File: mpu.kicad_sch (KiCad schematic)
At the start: 27 parts, among them J12 Conn_01x06, U2 STM32U585CIUxQ, Y1 ECS-160-8-36B2-CKM-TR, Y2 CM7V-T1A-32.768KHZ

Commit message: worked mainly on pcb
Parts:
- removed J12: Conn_01x06, Connector_PinHeader_2.54mm:PinHeader_1x06_P2.54mm_Vertical, symbol Connector_Generic:Conn_01x06
- added J13: Conn_01x04, Connector_PinHeader_2.54mm:PinHeader_1x04_P2.54mm_Vertical, symbol Connector_Generic:Conn_01x04
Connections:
- net servo1: now also J13.1 (Pin_1)
- net servo2: now also J13.2 (Pin_2)
- net servo3: now also J13.3 (Pin_3)
- net servo4: now also J13.4 (Pin_4)
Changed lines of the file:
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@@
 	(wire
 		(pts
-			(xy 163.83 76.2) (xy 163.83 77.47)
-		)
-		(stroke
-			(width 0)
-			(type default)
-		)
-	)
-	(wire
-		(pts
 			(xy 111.76 125.73) (xy 113.03 125.73)
 		)
@@
 	(wire
 		(pts
-			(xy 158.75 90.17) (xy 160.02 90.17)
-		)
-		(stroke
-			(width 0)
-			(type default)
-		)
-	)
-	(wire
-		(pts
 			(xy 109.22 80.01) (xy 113.03 80.01)
 		)
@@
 	(wire
 		(pts
-			(xy 163.83 93.98) (xy 163.83 90.17)
-		)
-		(stroke
-			(width 0)
-			(type default)
-		)
-	)
-	(wire
-		(pts
 			(xy 138.43 72.39) (xy 138.43 71.12)
 		)
@@
 	(wire
 		(pts
-			(xy 163.83 90.17) (xy 165.1 90.17)
-		)
-		(stroke
-			(width 0)
-			(type default)
-		)
-	)
-	(wire
-		(pts
 			(xy 58.42 87.63) (xy 58.42 92.71)
 		)
@@
 	(wire
 		(pts
-			(xy 140.97 49.53) (xy 140.97 50.8)
+			(xy 158.75 90.17) (xy 160.02 90.17)
 		)
 		(stroke
@@
 	(wire
 		(pts
-			(xy 138.43 71.12) (xy 138.43 62.23)
+			(xy 140.97 49.53) (xy 140.97 50.8)
 		)
 		(stroke
@@
 	(wire
 		(pts
-			(xy 133.35 43.18) (xy 135.89 43.18)
+			(xy 138.43 71.12) (xy 138.43 62.23)
 		)
 		(stroke
@@
 	(wire
 		(pts
-			(xy 67.31 93.98) (xy 67.31 95.25)
+			(xy 133.35 43.18) (xy 135.89 43.18)
 		)
 		(stroke
@@
 	(wire
 		(pts
-			(xy 128.27 71.12) (xy 128.27 72.39)
+			(xy 67.31 93.98) (xy 67.31 95.25)
 		)
 		(stroke
@@
 	(wire
 		(pts
-			(xy 113.03 100.33) (xy 111.76 100.33)
+			(xy 128.27 71.12) (xy 128.27 72.39)
 		)
 		(stroke
@@
 	(wire
 		(pts
-			(xy 111.76 110.49) (xy 113.03 110.49)
+			(xy 113.03 100.33) (xy 111.76 100.33)
 		)
 		(stroke
@@
 	(wire
 		(pts
-			(xy 163.83 77.47) (xy 165.1 77.47)
+			(xy 111.76 110.49) (xy 113.03 110.49)
 		)
 		(stroke
@@
 	)
 	(symbol
+		(lib_id "Connector_Generic:Conn_01x04")
+		(at 170.18 82.55 0)
+		(unit 1)
+		(exclude_from_sim no)
+		(in_bom yes)
+		(on_board yes)
+		(dnp no)
+		(fields_autoplaced yes)
+		(property "Reference" "J13"
+			(at 172.72 82.5499 0)
+			(effects
+				(font
+					(size 1.27 1.27)
+				)
+				(justify left)
+			)
+		)
+		(property "Value" "Conn_01x04"
+			(at 172.72 85.0899 0)
+			(effects
+				(font
+					(size 1.27 1.27)
+				)
+				(justify left)
+			)
+		)
+		(property "Footprint" "Connector_PinHeader_2.54mm:PinHeader_1x04_P2.54mm_Vertical"
+			(at 170.18 82.55 0)
+			(effects
+				(font
+					(size 1.27 1.27)
+				)
+				(hide yes)
+			)
+		)
+		(property "Datasheet" "~"
+			(at 170.18 82.55 0)
+			(effects
+				(font
+					(size 1.27 1.27)
+				)
+				(hide yes)
+			)
+		)
+		(property "Description" "Generic connector, single row, 01x04, script generated (kicad-library-utils/schlib/autogen/connector/)"
+			(at 170.18 82.55 0)
+			(effects
+				(font
+					(size 1.27 1.27)
+				)
+				(hide yes)
+			)
+		)
+		(pin "4"
+		)
+		(pin "2"
+		)
+		(pin "1"
+		)
+		(pin "3"
+		)
+		(instances
+			(project ""
+				(path "/d0cafa98-cc2a-4ab3-8dbc-f937bedf434b/94fda4c7-40dd-4c5d-acdd-b2f66ff666c2"
+					(reference "J13")
+					(unit 1)
+				)
+			)
+		)
+	)
+	(symbol
 		(lib_id "Connector_Generic:Conn_01x02")
 		(at 102.87 74.93 90)
@@
 	)
 	(symbol
-		(lib_id "power:+BATT")
-		(at 163.83 76.2 0)
-		(unit 1)
-		(exclude_from_sim no)
-		(in_bom yes)
-		(on_board yes)
-		(dnp no)
-		(fields_autoplaced yes)
-		(property "Reference" "#PWR029"
-			(at 163.83 80.01 0)
-			(effects
-				(font
-					(size 1.27 1.27)
-				)
-				(hide yes)
-			)
-		)
-		(property "Value" "+BATT"
-			(at 163.83 71.12 0)
-			(effects
-				(font
-					(size 1.27 1.27)
-				)
-			)
-		)
-		(property "Footprint" ""
-			(at 163.83 76.2 0)
-			(effects
-				(font
-					(size 1.27 1.27)
-				)
-				(hide yes)
-			)
-		)
-		(property "Datasheet" ""
-			(at 163.83 76.2 0)
-			(effects
-				(font
-					(size 1.27 1.27)
-				)
-				(hide yes)
-			)
-		)
-		(property "Description" "Power symbol creates a global label with name \"+BATT\""
-			(at 163.83 76.2 0)
-			(effects
-				(font
-					(size 1.27 1.27)
-				)
-				(hide yes)
-			)
-		)
-		(pin "1"
-		)
-		(instances
-			(project ""
-				(path "/d0cafa98-cc2a-4ab3-8dbc-f937bedf434b/94fda4c7-40dd-4c5d-acdd-b2f66ff666c2"
-					(reference "#PWR029")
-					(unit 1)
-				)
-			)
-		)
-	)
-	(symbol
 		(lib_id "Connector_Generic:Conn_01x02")
 		(at 69.85 100.33 270)
@@
 	)
 	(symbol
-		(lib_id "power:GND")
-		(at 163.83 93.98 0)
-		(unit 1)
-		(exclude_from_sim no)
-		(in_bom yes)
-		(on_board yes)
-		(dnp no)
-		(property "Reference" "#PWR090"
-			(at 163.83 100.33 0)
-			(effects
-				(font
-					(size 1.27 1.27)
-				)
-				(hide yes)
-			)
-		)
-		(property "Value" "GND"
-			(at 167.386 95.758 0)
-			(effects
-				(font
-					(size 1.27 1.27)
-				)
-			)
-		)
-		(property "Footprint" ""
-			(at 163.83 93.98 0)
-			(effects
-				(font
-					(size 1.27 1.27)
-				)
-				(hide yes)
-			)
-		)
-		(property "Datasheet" ""
-			(at 163.83 93.98 0)
-			(effects
-				(font
-					(size 1.27 1.27)
-				)
-				(hide yes)
-			)
-		)
-		(property "Description" "Power symbol creates a global label with name \"GND\" , ground"
-			(at 163.83 93.98 0)
-			(effects
-				(font
-					(size 1.27 1.27)
-				)
-				(hide yes)
-			)
-		)
-		(pin "1"
-		)
-		(instances
-			(project ""
-				(path "/d0cafa98-cc2a-4ab3-8dbc-f937bedf434b/94fda4c7-40dd-4c5d-acdd-b2f66ff666c2"
-					(reference "#PWR090")
-					(unit 1)
-				)
-			)
-		)
-	)
-	(symbol
 		(lib_id "ECS-160-8-36B2-CKM-TR:ECS-160-8-36B2-CKM-TR")
 		(at 91.44 85.09 180)
@@
 					(unit 1)
 				)
-			)
-		)
-	)
-	(symbol
-		(lib_id "Connector_Generic:Conn_01x06")
-		(at 170.18 82.55 0)
-		(unit 1)
-		(exclude_from_sim no)
-		(in_bom yes)
-		(on_board yes)
-		(dnp no)
-		(property "Reference" "J12"
-			(at 172.212 82.55 0)
-			(effects
-				(font
-					(size 1.27 1.27)
-				)
-				(justify left)
-			)
-		)
-		(property "Value" "Conn_01x06"
-			(at 172.212 85.09 0)
-			(effects
-				(font
-					(size 1.27 1.27)
-				)
-				(justify left)
-			)
-		)
-		(property "Footprint" "Connector_PinHeader_2.54mm:PinHeader_1x06_P2.54mm_Vertical"
-			(at 170.18 82.55 0)
-			(effects
-				(font
-					(size 1.27 1.27)
-				)
-				(hide yes)
-			)
-		)
-		(property "Datasheet" "~"
-			(at 170.18 82.55 0)
-			(effects
-				(font
-					(size 1.27 1.27)
-				)
-				(hide yes)
-			)
-		)
-		(property "Description" "Generic connector, single row, 01x06, script generated (kicad-library-utils/schlib/autogen/connector/)"
-			(at 170.18 82.55 0)
-			(effects
-				(font
-					(size 1.27 1.27)
-				)
-				(hide yes)
-			)
-		)
-		(pin "1"
-		)
-		(pin "6"
-		)
-		(pin "2"
-		)
-		(pin "4"
-		)
-		(pin "5"
-		)
-		(pin "3"
-		)
-		(instances
-			(project ""
-				(path "/d0cafa98-cc2a-4ab3-8dbc-f937bedf434b/94fda4c7-40dd-4c5d-acdd-b2f66ff666c2"
-					(reference "J12")
-					(unit 1)
-				)

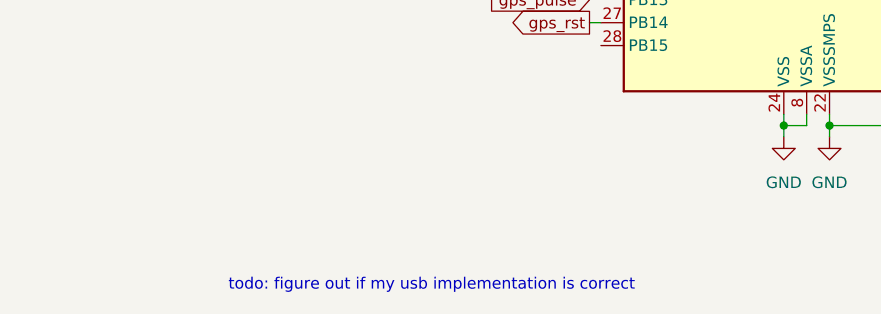
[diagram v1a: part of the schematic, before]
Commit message: basically just decoupling capacitors that I forgot
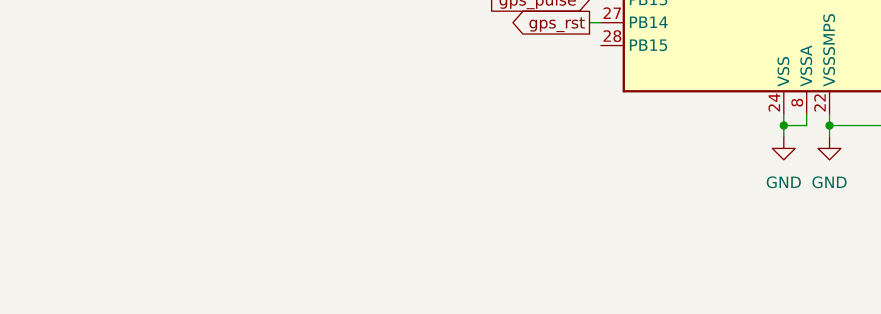
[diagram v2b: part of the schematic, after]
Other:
- note removed: "todo: figure out if my usb implementation is correct"
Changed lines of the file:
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@@
-		)
-	)
-	(text "todo: figure out if my usb implementation is correct\n"
-		(exclude_from_sim no)
-		(at 94.234 162.56 0)
-		(effects
-			(font
-				(size 1.27 1.27)
-			)
 		)
 	)

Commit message: almost done routing! getting pretty close to done now
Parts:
- U2: footprint Package_DFN_QFN:QFN-48-1EP_7x7mm_P0.5mm_EP5.6x5.6mm_ThermalVias -> Package_DFN_QFN:QFN-48-1EP_7x7mm_P0.5mm_EP5.6x5.6mm
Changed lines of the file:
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@@
 			)
 		)
-		(property "Footprint" "Package_DFN_QFN:QFN-48-1EP_7x7mm_P0.5mm_EP5.6x5.6mm_ThermalVias"
+		(property "Footprint" "Package_DFN_QFN:QFN-48-1EP_7x7mm_P0.5mm_EP5.6x5.6mm"
 			(at 115.57 140.97 0)
 			(effects

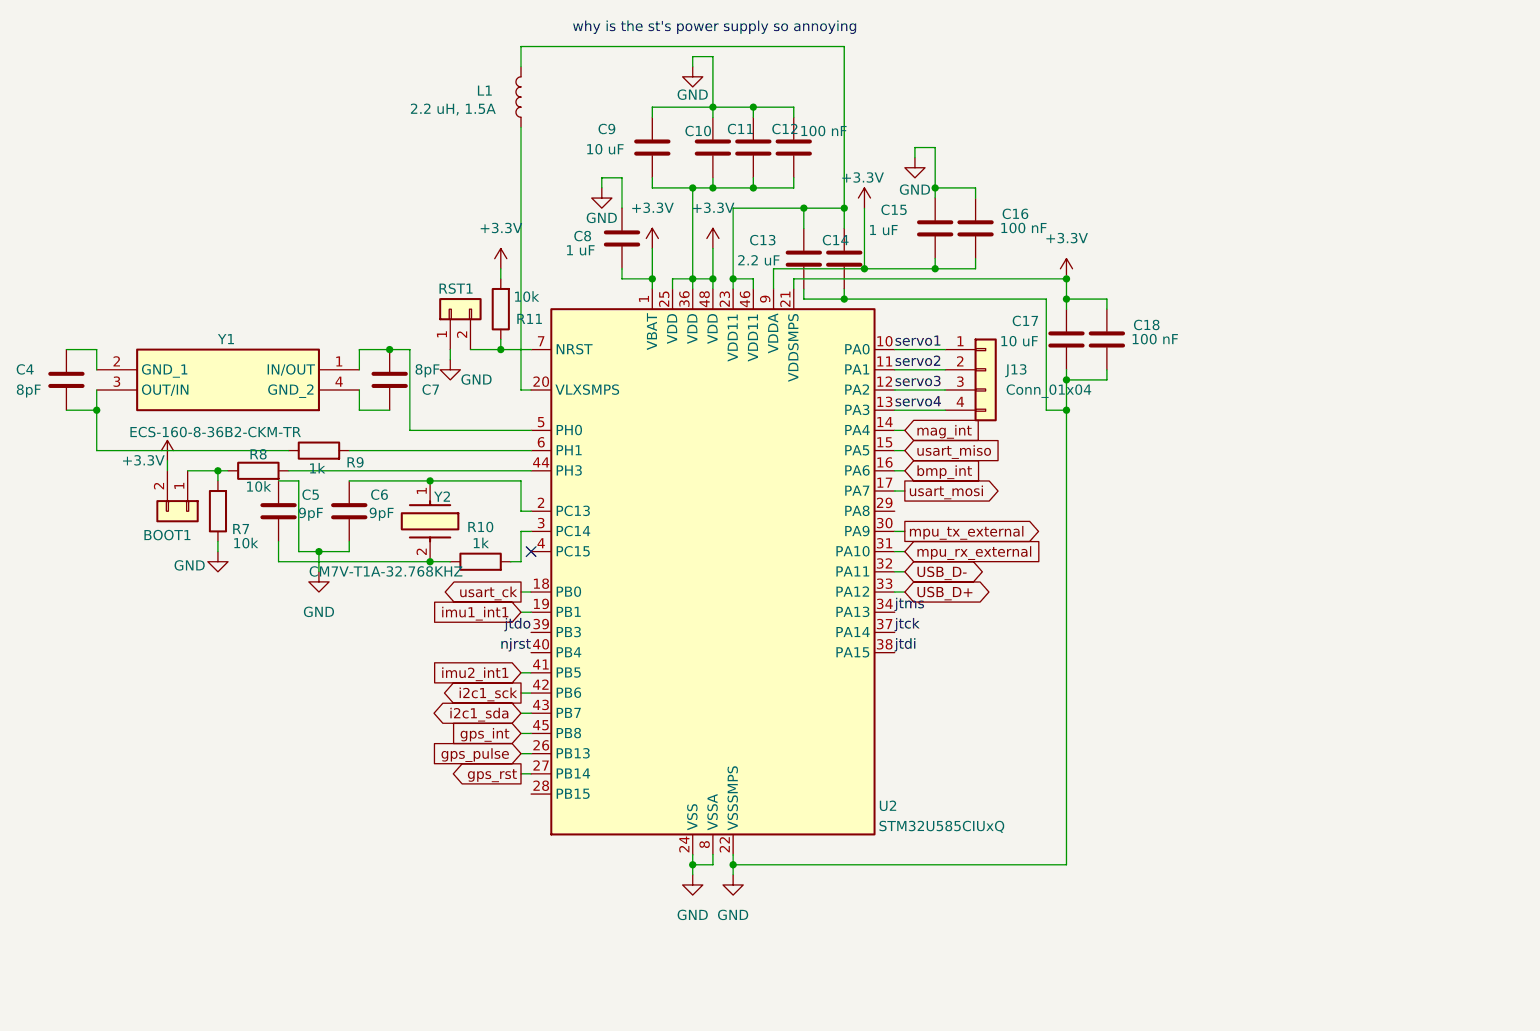
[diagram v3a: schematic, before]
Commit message: schematic updated - need to redo the layout now
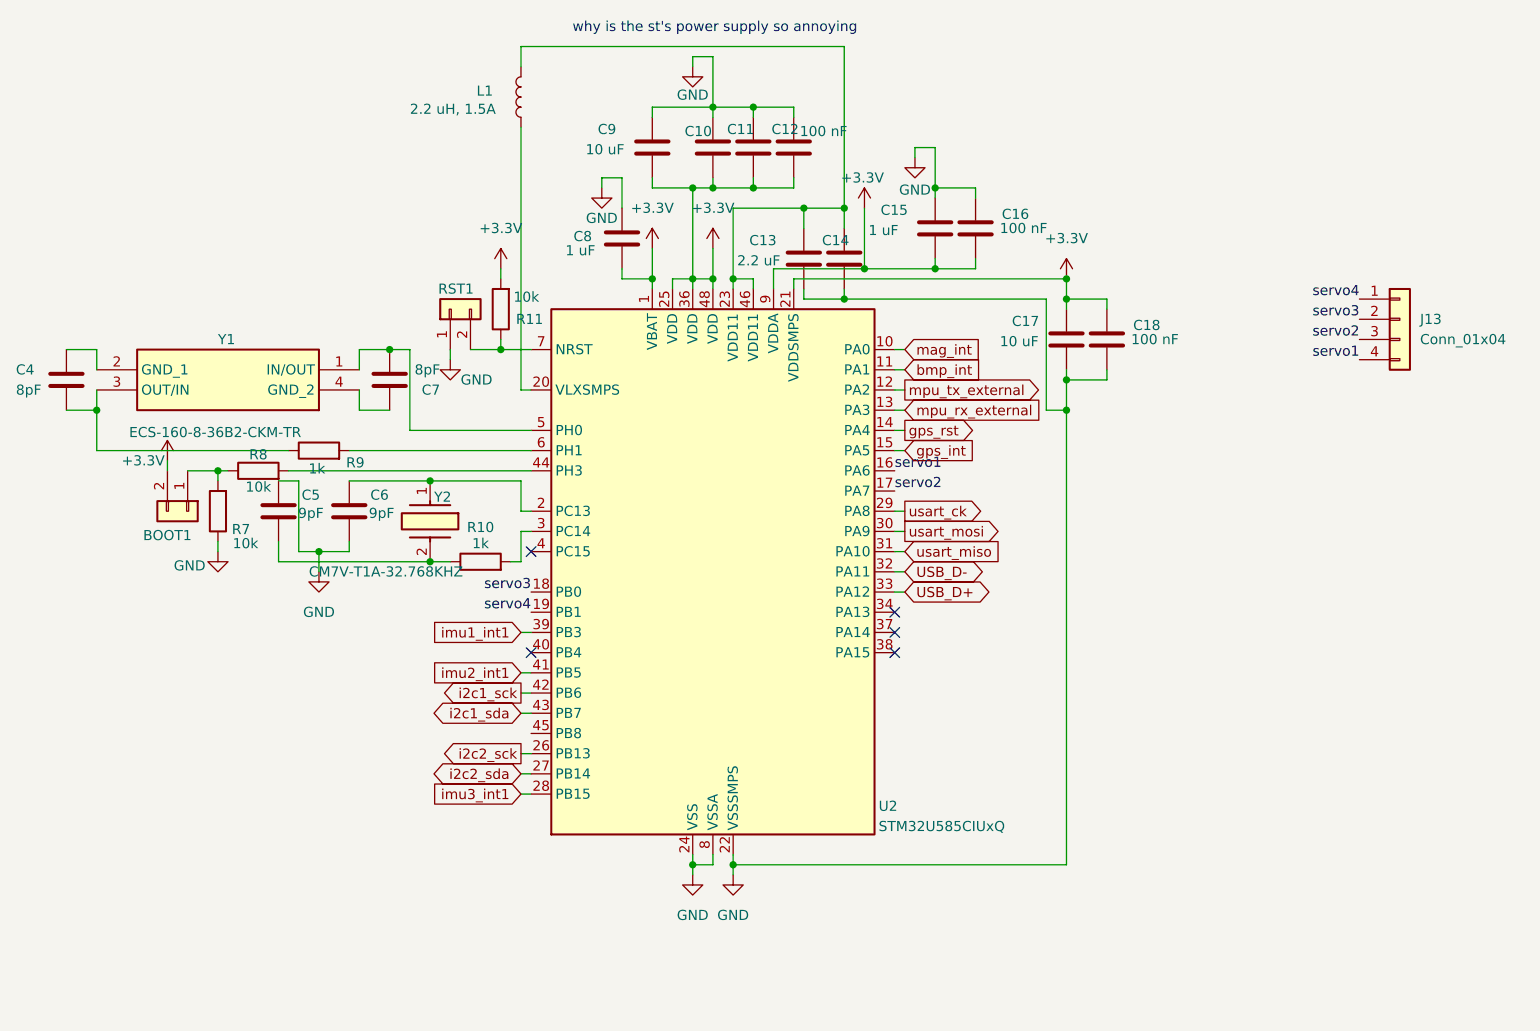
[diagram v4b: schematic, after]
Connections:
- net jtdo is gone; now on net imu1_int1: U2.39 (PB3)
- net bmp_int: now also U2.11 (PA1); no longer U2.16 (PA6)
- net gps_int: now also U2.15 (PA5); no longer U2.45 (PB8)
- net gps_rst: now also U2.14 (PA4); no longer U2.27 (PB14)
- net imu1_int1: no longer U2.19 (PB1)
- net mag_int: now also U2.10 (PA0); no longer U2.14 (PA4)
- net mpu_rx_external: now also U2.13 (PA3); no longer U2.31 (PA10)
- net mpu_tx_external: now also U2.12 (PA2); no longer U2.30 (PA9)
- net servo1: now also J13.4 (Pin_4), U2.16 (PA6); no longer J13.1 (Pin_1), U2.10 (PA0)
- net servo2: now also J13.3 (Pin_3), U2.17 (PA7); no longer J13.2 (Pin_2), U2.11 (PA1)
- net servo3: now also J13.2 (Pin_2), U2.18 (PB0); no longer J13.3 (Pin_3), U2.12 (PA2)
- net servo4: now also J13.1 (Pin_1), U2.19 (PB1); no longer J13.4 (Pin_4), U2.13 (PA3)
- net usart_ck: now also U2.29 (PA8); no longer U2.18 (PB0)
- net usart_miso: now also U2.31 (PA10); no longer U2.15 (PA5)
- net usart_mosi: now also U2.30 (PA9); no longer U2.17 (PA7)
- net imu3_int1: now reaches U2.28 (PB15)
- net gps_pulse renamed i2c2_sck
- net jtck: no longer names the net of U2.37 (PA14)
- net jtdi: no longer names the net of U2.38 (PA15)
- net jtms: no longer names the net of U2.34 (PA13)
- net njrst: no longer names the net of U2.40 (PB4)
- new net i2c2_sda: U2.27 (PB14)
- no-connect marks 1 -> 5
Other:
- moved on the sheet: J13

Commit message: started redoing layout for new pinout
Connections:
- net servo1: now also J13.1 (Pin_1); no longer J13.4 (Pin_4)
- net servo2: now also J13.2 (Pin_2); no longer J13.3 (Pin_3)
- net servo3: now also J13.3 (Pin_3); no longer J13.2 (Pin_2)
- net servo4: now also J13.4 (Pin_4); no longer J13.1 (Pin_1)
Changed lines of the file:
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@@
 	)
 	(label "servo1"
-		(at 217.17 81.28 180)
+		(at 217.17 73.66 180)
 		(effects
 			(font
@@
 	)
 	(label "servo4"
-		(at 217.17 73.66 180)
+		(at 217.17 81.28 180)
 		(effects
 			(font
@@
 	)
 	(label "servo3"
-		(at 217.17 76.2 180)
+		(at 217.17 78.74 180)
 		(effects
 			(font
@@
 	)
 	(label "servo2"
-		(at 217.17 78.74 180)
+		(at 217.17 76.2 180)
 		(effects
 			(font
